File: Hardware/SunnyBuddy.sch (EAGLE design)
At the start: 36 parts, among them J1 5.5x2.1mm Barrel, J2 POWER_JACKPTH, J5 M02PTH, J6 M023.5MM, J7 M023.5MM, J8 M023.5MM, U1 LT3652

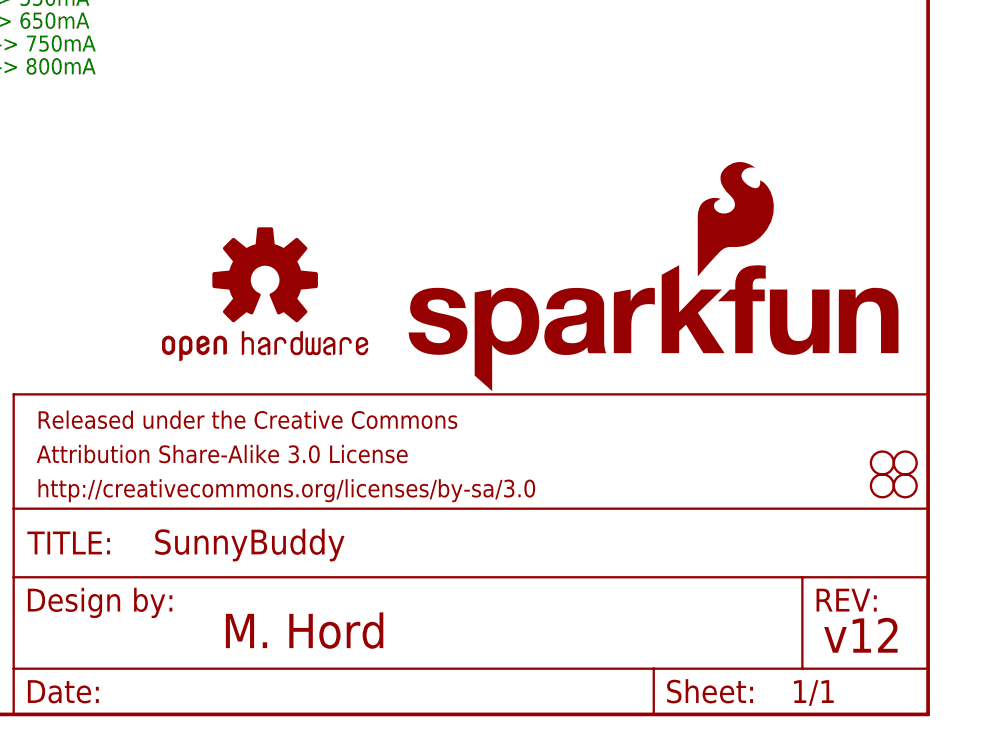
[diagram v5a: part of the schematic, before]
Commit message: Changes to silk, only, for production
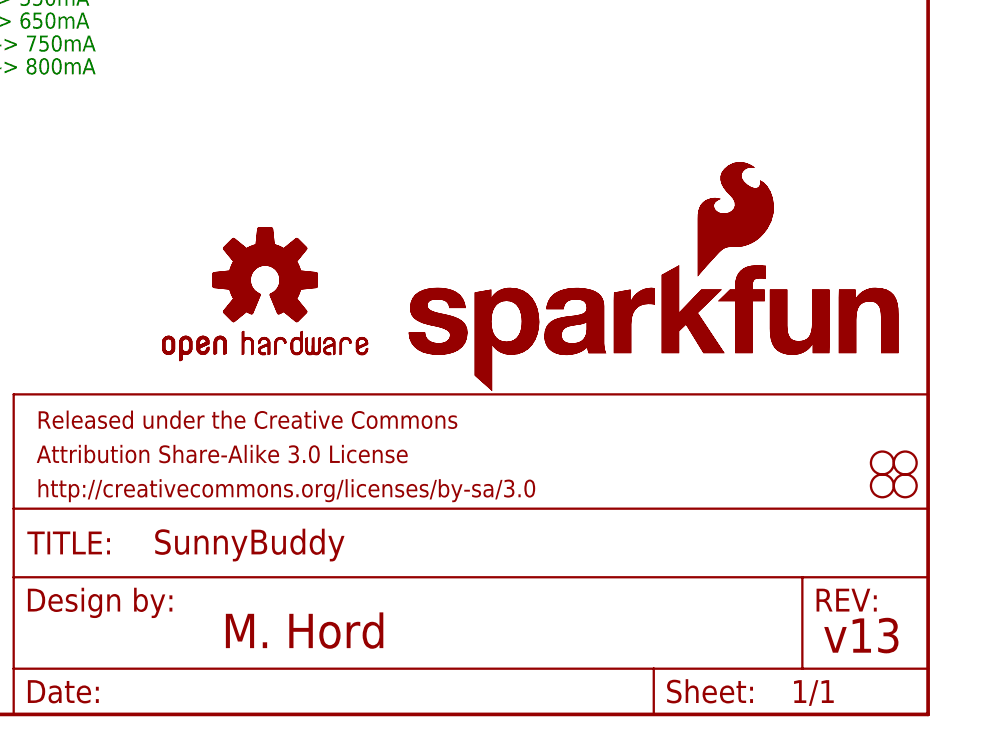
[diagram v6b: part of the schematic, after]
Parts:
- added LOGO3: OSHW-LOGOS, SparkFun-Aesthetics:OSHW-LOGOS
- added LOGO4: SFE_LOGO_NAME_FLAME.3_INCH, SparkFun-Aesthetics:SFE_LOGO_NAME_FLAME.3_INCH
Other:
- note added: "v13"
- note removed: "v12"
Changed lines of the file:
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@@
 <part name="JP4" library="SparkFun-Connectors" deviceset="M02" device="PTH" value="R_SEN"/>
 <part name="JP3" library="SparkFun-Passives" deviceset="JUMPER-PTH-2-NC" device=""/>
+<part name="LOGO3" library="SparkFun-Aesthetics" deviceset="OSHW-LOGO" device="S"/>
+<part name="LOGO4" library="SparkFun-Aesthetics" deviceset="SFE_LOGO_NAME_FLAME" device=".3_INCH"/>
 </parts>
 <sheets>
@@
 to your power source.
 You've been warned!</text>
-<text x="237.236" y="6.858" size="3.81" layer="94">v12</text>
+<text x="237.236" y="6.858" size="3.81" layer="94">v13</text>
 <text x="170.434" y="7.366" size="3.81" layer="94">M. Hord</text>
 <text x="167.894" y="147.828" size="1.778" layer="91">Cut the JP3 trace to
@@
 <attribute name="NAME" x="186.69" y="144.78" size="1.778" layer="95" rot="R180"/>
 </instance>
+<instance part="LOGO3" gate="G$1" x="175.26" y="48.26"/>
+<instance part="LOGO4" gate="G$1" x="190.5" y="35.56"/>
 </instances>
 <busses>
